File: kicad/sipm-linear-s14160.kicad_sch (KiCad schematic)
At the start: 13 parts, among them J1 SSQ-103-01-G-D, J18 SSQ-103-01-G-D, U2 S15643

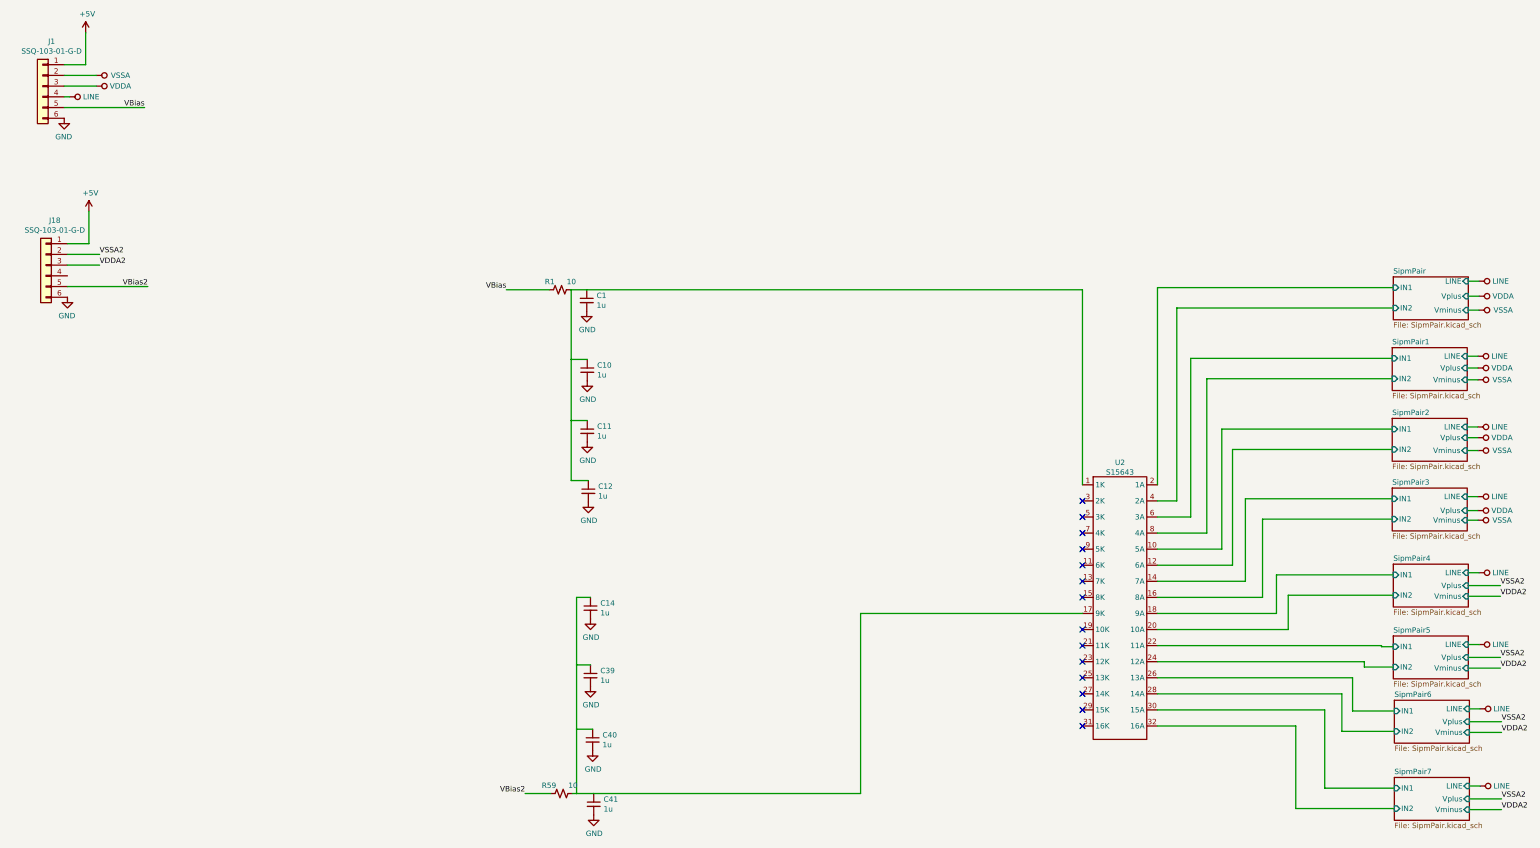
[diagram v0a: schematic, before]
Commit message: Check in before removing feedback cap
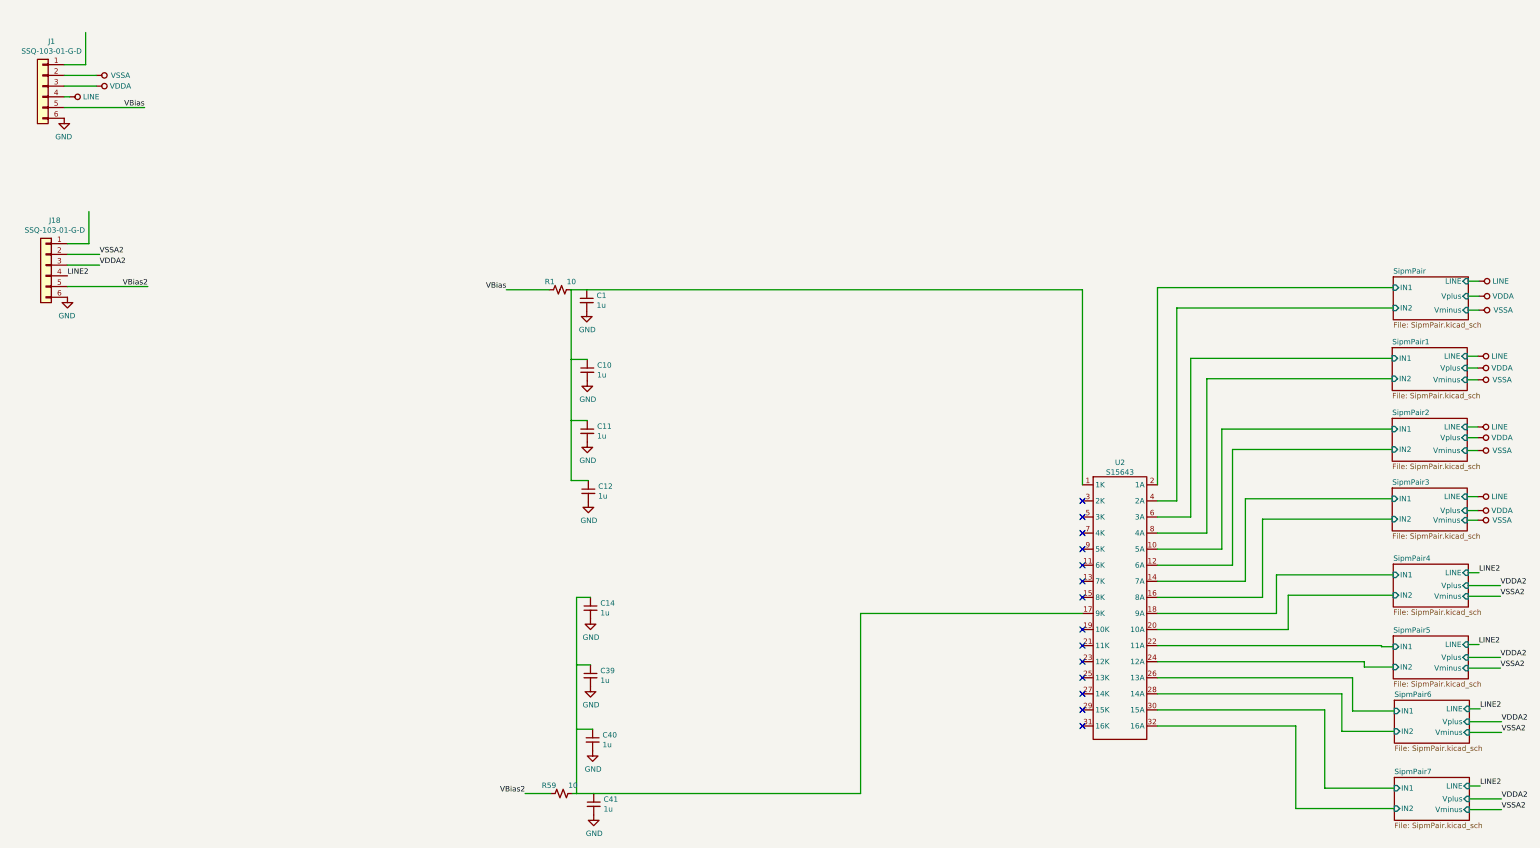
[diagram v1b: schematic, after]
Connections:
- net LINE2: now reaches J18.4 (Pin_4)
- net +5V: no longer names the net of J18.1 (Pin_1)
- net +5V: no longer J1.1 (Pin_1)

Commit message: Change decoupling to 1206
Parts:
- C1, C10, C11, C12, C14, C39, C40, C41: footprint Capacitor_SMD:C_0805_2012Metric -> Capacitor_SMD:C_1206_3216Metric
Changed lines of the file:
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@@
       (effects (font (size 1.27 1.27)) (justify left))
     )
-    (property "Footprint" "Capacitor_SMD:C_0805_2012Metric" (id 2) (at 167.132 123.19 0)
+    (property "Footprint" "Capacitor_SMD:C_1206_3216Metric" (id 2) (at 167.132 123.19 0)
       (effects (font (size 1.27 1.27)) hide)
     )
@@
       (effects (font (size 1.27 1.27)) (justify left))
     )
-    (property "Footprint" "Capacitor_SMD:C_0805_2012Metric" (id 2) (at 167.894 179.578 0)
+    (property "Footprint" "Capacitor_SMD:C_1206_3216Metric" (id 2) (at 167.894 179.578 0)
       (effects (font (size 1.27 1.27)) hide)
     )
@@
       (effects (font (size 1.27 1.27)) (justify left))
     )
-    (property "Footprint" "Capacitor_SMD:C_0805_2012Metric" (id 2) (at 168.402 210.82 0)
+    (property "Footprint" "Capacitor_SMD:C_1206_3216Metric" (id 2) (at 168.402 210.82 0)
       (effects (font (size 1.27 1.27)) hide)
     )
@@
       (effects (font (size 1.27 1.27)) (justify left))
     )
-    (property "Footprint" "Capacitor_SMD:C_0805_2012Metric" (id 2) (at 167.894 195.58 0)
+    (property "Footprint" "Capacitor_SMD:C_1206_3216Metric" (id 2) (at 167.894 195.58 0)
       (effects (font (size 1.27 1.27)) hide)
     )
@@
       (effects (font (size 1.27 1.27)) (justify left))
     )
-    (property "Footprint" "Capacitor_SMD:C_0805_2012Metric" (id 2) (at 167.132 137.668 0)
+    (property "Footprint" "Capacitor_SMD:C_1206_3216Metric" (id 2) (at 167.132 137.668 0)
       (effects (font (size 1.27 1.27)) hide)
     )
@@
       (effects (font (size 1.27 1.27)) (justify left))
     )
-    (property "Footprint" "Capacitor_SMD:C_0805_2012Metric" (id 2) (at 167.005 106.68 0)
+    (property "Footprint" "Capacitor_SMD:C_1206_3216Metric" (id 2) (at 167.005 106.68 0)
       (effects (font (size 1.27 1.27)) hide)
     )
@@
       (effects (font (size 1.27 1.27)) (justify left))
     )
-    (property "Footprint" "Capacitor_SMD:C_0805_2012Metric" (id 2) (at 168.656 226.06 0)
+    (property "Footprint" "Capacitor_SMD:C_1206_3216Metric" (id 2) (at 168.656 226.06 0)
       (effects (font (size 1.27 1.27)) hide)
     )
@@
       (effects (font (size 1.27 1.27)) (justify left))
     )
-    (property "Footprint" "Capacitor_SMD:C_0805_2012Metric" (id 2) (at 167.386 151.892 0)
+    (property "Footprint" "Capacitor_SMD:C_1206_3216Metric" (id 2) (at 167.386 151.892 0)
       (effects (font (size 1.27 1.27)) hide)
     )
@@
     )
     (path "/cdb77805-3e2e-4482-9783-8c9b61e37144"
-      (reference "C1") (unit 1) (value "1u") (footprint "Capacitor_SMD:C_0805_2012Metric")
+      (reference "C1") (unit 1) (value "1u") (footprint "Capacitor_SMD:C_1206_3216Metric")
     )
     (path "/6b5475ad-5d86-4470-948c-5137d38de55c/ed92220c-06d5-4c73-9e7d-257765c2f0d0"
@@
     )
     (path "/1a59b087-f9c5-4376-8902-1885ee68ce5f"
-      (reference "C10") (unit 1) (value "1u") (footprint "Capacitor_SMD:C_0805_2012Metric")
+      (reference "C10") (unit 1) (value "1u") (footprint "Capacitor_SMD:C_1206_3216Metric")
     )
     (path "/a3813db4-79ad-4cc1-89eb-d62e44ec460e"
-      (reference "C11") (unit 1) (value "1u") (footprint "Capacitor_SMD:C_0805_2012Metric")
+      (reference "C11") (unit 1) (value "1u") (footprint "Capacitor_SMD:C_1206_3216Metric")
     )
     (path "/d617840c-3540-430e-83bc-704bd708588d"
-      (reference "C12") (unit 1) (value "1u") (footprint "Capacitor_SMD:C_0805_2012Metric")
+      (reference "C12") (unit 1) (value "1u") (footprint "Capacitor_SMD:C_1206_3216Metric")
     )
     (path "/355a41b9-f4c7-4931-a25a-aab8105d2d98"
-      (reference "C14") (unit 1) (value "1u") (footprint "Capacitor_SMD:C_0805_2012Metric")
+      (reference "C14") (unit 1) (value "1u") (footprint "Capacitor_SMD:C_1206_3216Metric")
     )
     (path "/604e08ef-cafa-4ea2-be34-754269f1dc0e/ed92220c-06d5-4c73-9e7d-257765c2f0d0"
@@
     )
     (path "/73dc4007-186a-4140-aa1e-2e32742db85b"
-      (reference "C39") (unit 1) (value "1u") (footprint "Capacitor_SMD:C_0805_2012Metric")
+      (reference "C39") (unit 1) (value "1u") (footprint "Capacitor_SMD:C_1206_3216Metric")
     )
     (path "/5a420af9-1c85-4a24-a1ea-75e2ec293f94"
-      (reference "C40") (unit 1) (value "1u") (footprint "Capacitor_SMD:C_0805_2012Metric")
+      (reference "C40") (unit 1) (value "1u") (footprint "Capacitor_SMD:C_1206_3216Metric")
     )
     (path "/d3399dd4-8a78-4023-bfb1-9a29c674906a"
-      (reference "C41") (unit 1) (value "1u") (footprint "Capacitor_SMD:C_0805_2012Metric")
+      (reference "C41") (unit 1) (value "1u") (footprint "Capacitor_SMD:C_1206_3216Metric")
     )
     (path "/92a3b03c-a0af-41c5-b0fa-080612e6db63/ed92220c-06d5-4c73-9e7d-257765c2f0d0"

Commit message: Fix track under drill hole
Pretty sure JLCPCB quietly fixed this for us on the initial design.
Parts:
- C1, C10, C11, C12, C14, C39, C40, C41: Voltage (none) -> 100V
